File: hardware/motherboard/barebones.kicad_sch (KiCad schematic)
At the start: 0 parts

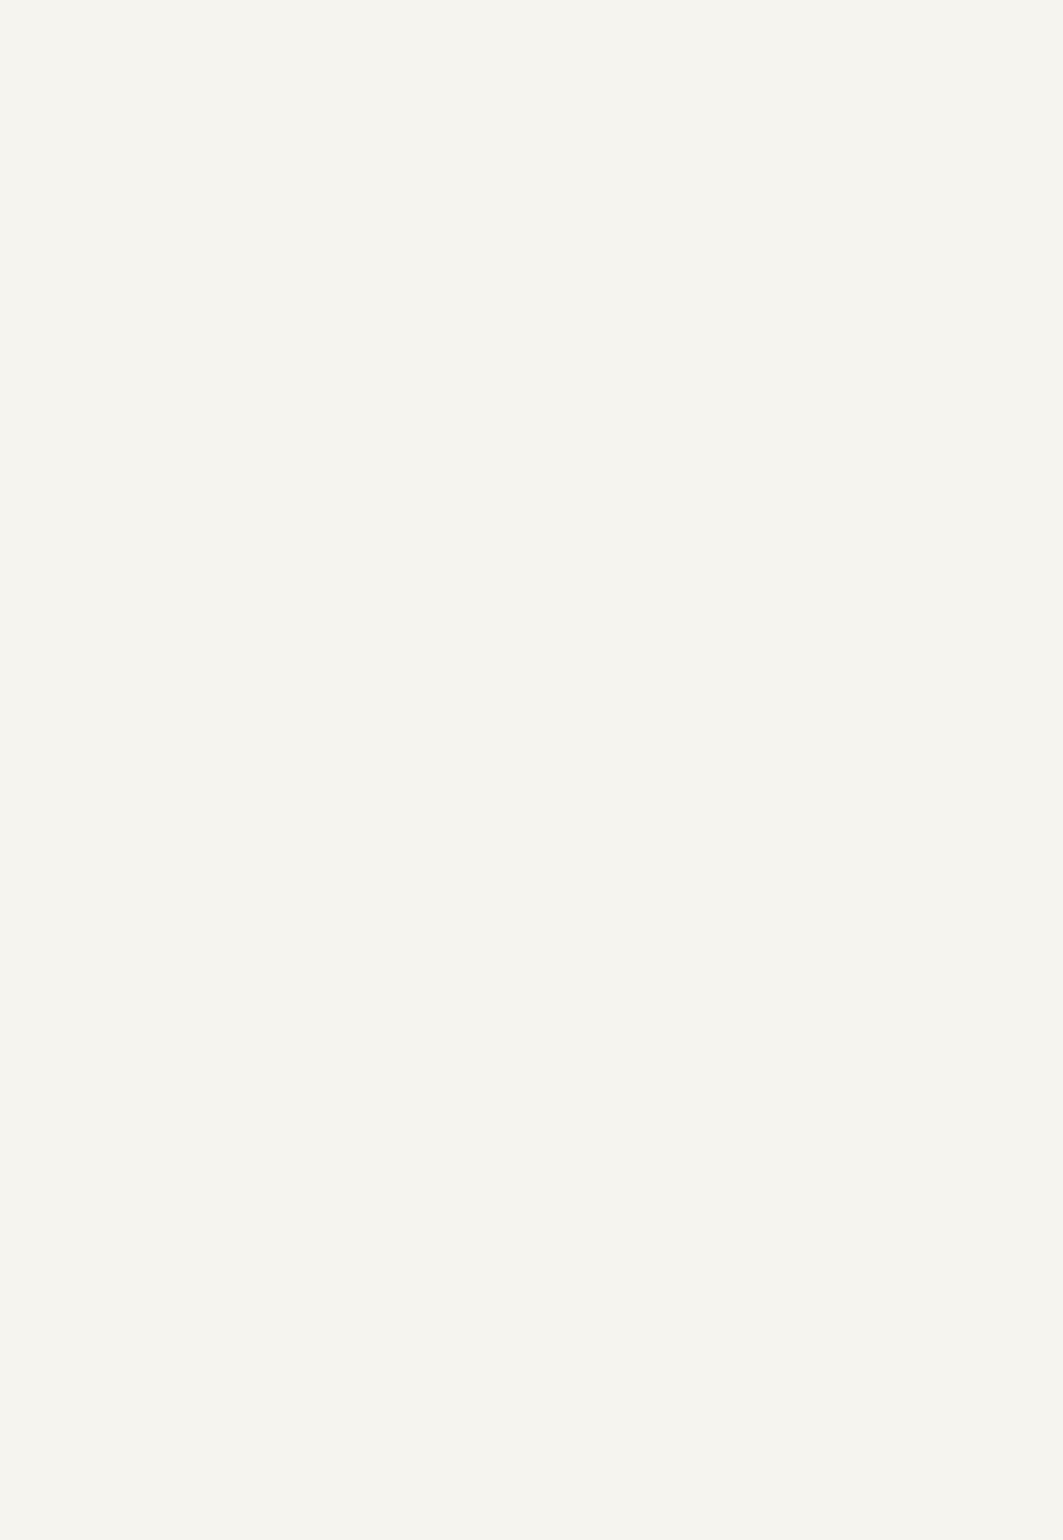
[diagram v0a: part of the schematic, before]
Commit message: pushed many changes and added dedicated bms module
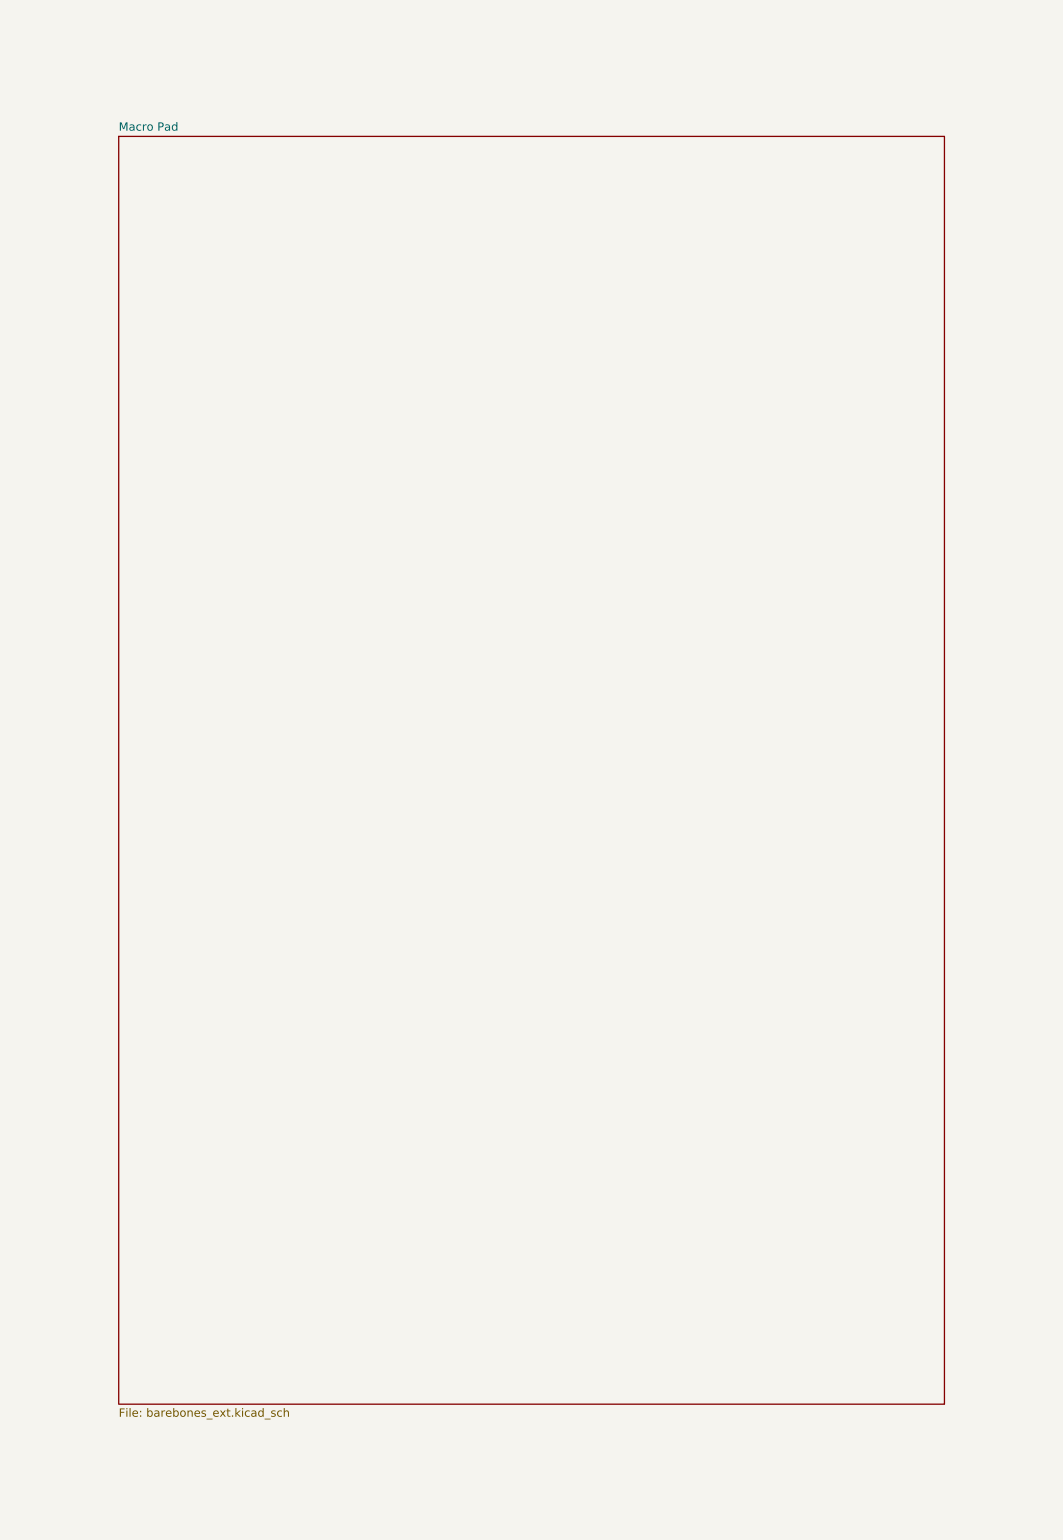
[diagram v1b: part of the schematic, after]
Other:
- added sheet Macro Pad (barebones_ext.kicad_sch)
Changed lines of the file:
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@@
+	)
+	(sheet
+		(at 469.9 403.86)
+		(size 125.73 193.04)
+		(exclude_from_sim no)
+		(in_bom yes)
+		(on_board yes)
+		(dnp no)
+		(fields_autoplaced yes)
+		(stroke
+			(width 0.1524)
+			(type solid)
+		)
+		(fill
+			(color 0 0 0 0)
+		)
+		(property "Sheetname" "Macro Pad"
+			(at 469.9 403.1484 0)
+			(show_name no)
+			(do_not_autoplace no)
+			(effects
+				(font
+					(size 1.27 1.27)
+				)
+				(justify left bottom)
+			)
+		)
+		(property "Sheetfile" "barebones_ext.kicad_sch"
+			(at 469.9 597.4846 0)
+			(show_name no)
+			(do_not_autoplace no)
+			(effects
+				(font
+					(size 1.27 1.27)
+				)
+				(justify left top)
+			)
+		)
+		(instances
+			(project "barebones"
+				(path "/55e8bb80-206a-472b-ac89-6555b6c3d282"
+					(page "8")
+				)
+			)
+		)
 	)
 	(sheet

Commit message: connected hierarchical labels with net labels in the root sheet
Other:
- sheet Embedded Controller and Internal Audio ports: added BACKLIGHT_PWM, BUCK_PWRON, CAPS_P, CHARGE_CNTRL, CHRG_12C_SCL, CHRG_12C_SDA, CHRG_OK_EC, CHRG_PROT, HALL_SENSE, I2C1_SCL_EC, I2C1_SCL_M2, I2C1_SDA_EC, I2C1_SDA_M2, I2C7_SCL_M0, I2C7_SDA_M0, I2S0_LRCK, I2S0_MLCK, I2S0_SCLK, I2S0_SDI0, I2S0_SDO0, INT_AUDIO, KSI0, KSI1, KSI2, KSI3, KSI4, KSI5, KSI6, KSI7, KSO0, KSO1, KSO10, KSO11, KSO12, KSO13, KSO14, KSO15, KSO2, KSO3, KSO4, KSO5, KSO6, KSO7, KSO8, KSO9, MIC_PRESENT, PWRON_RK, RESETB_RK, SMBC_BATT, SMBD_BATT, SPK_MUTE, USB_CTRL_RESET_1, USB_CTRL_RESET_2, USB_SIG_STAT; removed none
- sheet High Speed IO ports: added CPU_BIG0_VSEL, CPU_BIG1_VSEL, DDR_CH1_CK_C, DDR_CH1_CK_D, DDR_CH1_DM0_C, DDR_CH1_DM0_D, DDR_CH1_DM1_C, DDR_CH1_DM1_D, DDR_CH1_DQ0_C, DDR_CH1_DQ0_D, DDR_CH1_DQ10_C, DDR_CH1_DQ10_D, DDR_CH1_DQ11_C, DDR_CH1_DQ11_D, DDR_CH1_DQ12_C, DDR_CH1_DQ12_D, DDR_CH1_DQ13_C, DDR_CH1_DQ13_D, DDR_CH1_DQ14_C, DDR_CH1_DQ14_D, DDR_CH1_DQ15_C, DDR_CH1_DQ15_D, DDR_CH1_DQ1_C, DDR_CH1_DQ1_D, DDR_CH1_DQ2_C, DDR_CH1_DQ2_D, DDR_CH1_DQ3_C, DDR_CH1_DQ3_D, DDR_CH1_DQ4_C, DDR_CH1_DQ4_D, DDR_CH1_DQ5_C, DDR_CH1_DQ5_D, DDR_CH1_DQ6_C, DDR_CH1_DQ6_D, DDR_CH1_DQ7_C, DDR_CH1_DQ7_D, DDR_CH1_DQ8_C, DDR_CH1_DQ8_D, DDR_CH1_DQ9_C, DDR_CH1_DQ9_D, DDR_CH1_DQS0N_C, DDR_CH1_DQS0N_D, DDR_CH1_DQS0P_C, DDR_CH1_DQS0P_D, DDR_CH1_DQS1N_C, DDR_CH1_DQS1N_D, DDR_CH1_DQS1P_C, DDR_CH1_DQS1P_D, DDR_CH1_LP4/4X_CKE0/LP5_CS0_C, DDR_CH1_LP4/4X_CKE0/LP5_CS0_D, DDR_CH1_LP4/4X_CKE1/LP5_CS1_C, DDR_CH1_LP4/4X_CKE1/LP5_CS1_D, DDR_CH1_LP4/4X_CS0_C, DDR_CH1_LP4/4X_CS0_D, DDR_CH1_LP4/4X_CS1_C, DDR_CH1_LP4/4X_CS1_D, DDR_RESET, EDP_TX0_HDP, FSPI-CLK, FSPI-CS0, FSPI-D0, FSPI-D1, FSPI-D2, FSPI-D3, GPIO3_B3_U, GPIO3_B4_U, GPIO3_B5_U, HDMI0_TX0N_PORT/eDP0_TX_D0N, HDMI0_TX0P_PORT/eDP0_TX_D0P, HDMI0_TX1N_PORT/eDP0_TX_D1N, HDMI0_TX1P_PORT/eDP0_TX_D1P, HDMI0_TX2N_PORT/eDP0_TX_D2N, HDMI0_TX2P_PORT/eDP0_TX_D2P, HDMI0_TX3N_PORT/eDP0_TX_D3N, HDMI0_TX3P_PORT/eDP0_TX_D3P, HDMI1_TX0N_PORT/eDP1_TX_D0N, HDMI1_TX0P_PORT/eDP1_TX_D0P, HDMI1_TX1N_PORT/eDP1_TX_D1N, HDMI1_TX1P_PORT/eDP1_TX_D1P, HDMI1_TX2N_PORT/eDP1_TX_D2N, HDMI1_TX2P_PORT/eDP1_TX_D2P, HDMI1_TX3N_PORT/eDP1_TX_D3N, HDMI1_TX3P_PORT/eDP1_TX_D3P, HDMI1_TX_ON_H, HDMI1_TX_SBDN/eDP1_TX_AUXN, HDMI1_TX_SBDP/eDP1_TX_AUXP, HDMITX1_CEC_M2, HDMITX1_HPDIN_M1, HDMITX1_SCL_M1, HDMITX1_SDA_M1, HP_DETECT, HP_INT, I2C0_SCL_M2, I2C0_SDA_M2, I2C1_SCL_M0, I2C1_SDA_M0, I2C4_SCL_M1, I2C4_SDA_M1, I2C4_SDA_M3, I2C5_SCL_M4, I2C5_SDA_M4, I2C7_SCL_M0, I2C7_SDA_M0, I2S0_LRCK_TX, I2S0_MLCK, I2S0_SCLK_TX, I2S0_SDI0, I2S0_SDO0, NPU_VSEL, PCIE20_0_REFCLKN, PCIE20_0_REFCLKP, PCIE20_0_RXN, PCIE20_0_RXP, PCIE20_0_TXN, PCIE20_0_TXP, PCIE30X1_0_CLKREQn_M1_L, PCIE30X1_0_PERSTn_M1_L, PCIE30X1_0_WAKEn_M1_L, PCIE30X2_CLKREQn_M1, PCIE30X2_PERSTn_M1, PCIE30X2_WAKEn_M1, PCIE30X4_CLKREQn_M1_L, PCIE30X4_PERSTn_M1_L, PCIE30X4_PWREN_H, PCIE30X4_WAKEn_M1_L, PCIE30_PORT0_REF_CLKN, PCIE30_PORT0_REF_CLKP, PCIE30_PORT0_RX0N, PCIE30_PORT0_RX0P, PCIE30_PORT0_RX1N, PCIE30_PORT0_RX1P, PCIE30_PORT0_TX0N, PCIE30_PORT0_TX0P, PCIE30_PORT0_TX1N, PCIE30_PORT0_TX1P, PCIE30_PORT1_REF_CLKN, PCIE30_PORT1_REF_CLKP, PCIE30_PORT1_RX0N, PCIE30_PORT1_RX0P, PCIE30_PORT1_RX1N, PCIE30_PORT1_RX1P, PCIE30_PORT1_TX0N, PCIE30_PORT1_TX0P, PCIE30_PORT1_TX1N, PCIE30_PORT1_TX1P, PMIC_INT_L, PMIC_SLEEP1, PWRCTRL2_PMIC, PWRCTRL3_PMIC, RESETB, RTC_CLK_EN, SDMMC_CLK, SDMMC_CMD, SDMMC_DAT0, SDMMC_DAT1, SDMMC_DAT2, SDMMC_DAT3, SDMMC_DET, SPI2_CLK_M2, SPI2_CS0_M2, SPI2_MOSI_M2, USB20_HOST0_DM, USB20_HOST0_DP, USB20_HOST1_DM, USB20_HOST1_DP, USB30_2_SSRXN, USB30_2_SSRXP, USB30_2_SSTXN, USB30_2_SSTXP, USB_1_OTG_DM, USB_1_OTG_DP, USB_1_RX1N, USB_1_RX1P, USB_1_RX2N, USB_1_RX2P, USB_1_SBU1, USB_1_SBU1_DC, USB_1_SBU2, USB_1_TX1N, USB_1_TX1P, USB_1_TX2N, USB_1_TX2P, USB_2_OTG_DM, USB_2_OTG_DP, USB_2_RX1N, USB_2_RX1P, USB_2_RX2N, USB_2_RX2P, USB_2_SBU1, USB_2_SBU1_DC, USB_2_SBU2, USB_2_TX1N, USB_2_TX1P, USB_2_TX2N, USB_2_TX2P; removed none
- sheet Macro Pad ports: added USB_MACRO_DN, USB_MACRO_DP; removed none
- sheet Memory Subsystem(LPDDR4x) ports: added DDR_CH0_A0_A, DDR_CH0_A0_B, DDR_CH0_A1_A, DDR_CH0_A1_B, DDR_CH0_A2_A, DDR_CH0_A2_B, DDR_CH0_A3_A, DDR_CH0_A3_B, DDR_CH0_A4_A, DDR_CH0_A4_B, DDR_CH0_A5_A, DDR_CH0_A5_B, DDR_CH0_CKB_A, DDR_CH0_CKB_B, DDR_CH0_CK_A, DDR_CH0_CK_B, DDR_CH0_DM0_A, DDR_CH0_DM0_B, DDR_CH0_DM1_A, DDR_CH0_DM1_B, DDR_CH0_DQ0_A, DDR_CH0_DQ0_B, DDR_CH0_DQ10_A, DDR_CH0_DQ10_B, DDR_CH0_DQ11_A, DDR_CH0_DQ11_B, DDR_CH0_DQ12_A, DDR_CH0_DQ12_B, DDR_CH0_DQ13_A, DDR_CH0_DQ13_B, DDR_CH0_DQ14_A, DDR_CH0_DQ14_B, DDR_CH0_DQ15_A, DDR_CH0_DQ15_B, DDR_CH0_DQ1_A, DDR_CH0_DQ1_B, DDR_CH0_DQ2_A, DDR_CH0_DQ2_B, DDR_CH0_DQ3_A, DDR_CH0_DQ3_B, DDR_CH0_DQ4_A, DDR_CH0_DQ4_B, DDR_CH0_DQ5_A, DDR_CH0_DQ5_B, DDR_CH0_DQ6_A, DDR_CH0_DQ6_B, DDR_CH0_DQ7_A, DDR_CH0_DQ7_B, DDR_CH0_DQ8_A, DDR_CH0_DQ8_B, DDR_CH0_DQ9_A, DDR_CH0_DQ9_B, DDR_CH0_DQS0N_A, DDR_CH0_DQS0N_B, DDR_CH0_DQS0P_A, DDR_CH0_DQS0P_B, DDR_CH0_DQS1N_A, DDR_CH0_DQS1N_B, DDR_CH0_DQS1P_A, DDR_CH0_DQS1P_B, DDR_CH0_LP4/4X_CKE0/LP5_CS0_A, DDR_CH0_LP4/4X_CKE0/LP5_CS0_B, DDR_CH0_LP4/4X_CKE1/LP5_CS1_A, DDR_CH0_LP4/4X_CKE1/LP5_CS1_B, DDR_CH0_LP4/4X_CS0_A, DDR_CH0_LP4/4X_CS0_B, DDR_CH0_LP4/4X_CS1_A, DDR_CH0_LP4/4X_CS1_B, DDR_CH1_A0_C, DDR_CH1_A0_D, DDR_CH1_A1_C, DDR_CH1_A1_D, DDR_CH1_A2_C, DDR_CH1_A2_D, DDR_CH1_A3_C, DDR_CH1_A3_D, DDR_CH1_A4_C, DDR_CH1_A4_D, DDR_CH1_A5_C, DDR_CH1_A5_D, DDR_CH1_CKB_C, DDR_CH1_CKB_D, DDR_CH1_CK_C, DDR_CH1_CK_D, DDR_CH1_DM0_C, DDR_CH1_DM0_D, DDR_CH1_DM1_C, DDR_CH1_DM1_D, DDR_CH1_DQ0_C, DDR_CH1_DQ0_D, DDR_CH1_DQ10_C, DDR_CH1_DQ10_D, DDR_CH1_DQ11_C, DDR_CH1_DQ11_D, DDR_CH1_DQ12_C, DDR_CH1_DQ12_D, DDR_CH1_DQ13_C, DDR_CH1_DQ13_D, DDR_CH1_DQ14_C, DDR_CH1_DQ14_D, DDR_CH1_DQ15_C, DDR_CH1_DQ15_D, DDR_CH1_DQ1_C, DDR_CH1_DQ1_D, DDR_CH1_DQ2_C, DDR_CH1_DQ2_D, DDR_CH1_DQ3_C, DDR_CH1_DQ3_D, DDR_CH1_DQ4_C, DDR_CH1_DQ4_D, DDR_CH1_DQ5_C, DDR_CH1_DQ5_D, DDR_CH1_DQ6_C, DDR_CH1_DQ6_D, DDR_CH1_DQ7_C, DDR_CH1_DQ7_D, DDR_CH1_DQ8_C, DDR_CH1_DQ8_D, DDR_CH1_DQ9_C, DDR_CH1_DQ9_D, DDR_CH1_DQS0N_C, DDR_CH1_DQS0N_D, DDR_CH1_DQS0P_C, DDR_CH1_DQS0P_D, DDR_CH1_DQS1N_C, DDR_CH1_DQS1N_D, DDR_CH1_DQS1P_C, DDR_CH1_DQS1P_D, DDR_CH1_LP4/4X_CKE0/LP5_CS0_C, DDR_CH1_LP4/4X_CKE0/LP5_CS0_D, DDR_CH1_LP4/4X_CKE1/LP5_CS1_C, DDR_CH1_LP4/4X_CKE1/LP5_CS1_D, DDR_CH1_LP4/4X_CS0_C, DDR_CH1_LP4/4X_CS0_D, DDR_CH1_LP4/4X_CS1_C, DDR_CH1_LP4/4X_CS1_D, DDR_RESET; removed none
- sheet Memory and Control ports: added FSPI-CLK, FSPI-CS0, FSPI-D0, FSPI-D1, FSPI-D2, FSPI-D3, HALL_SENSE_0, I2C1_SCL_M2, I2C1_SDA_M2, LP_INDICATOR, RTC_CLK_EN; removed none
- sheet Peripheral IO Connectors ports: added 12C1_EXTI_EC, BACKLIGHT_DN, BACKLIGHT_DP, BOARD_ID, CAPS_N, CAPS_P, EC_CONTROL, EDP_TX0_AUX_N, EDP_TX0_AUX_P, EDP_TX0_BL_EN, EDP_TX0_BL_PWM, EDP_TX0_HDP, GPIO3_B5_U, HDMI0_TX0N_PORT/eDP0_TX_D0N, HDMI0_TX0P_PORT/eDP0_TX_D0P, HDMI0_TX1N_PORT/eDP0_TX_D1N, HDMI0_TX1P_PORT/eDP0_TX_D1P, HDMI0_TX2N_PORT/eDP0_TX_D2N, HDMI0_TX2P_PORT/eDP0_TX_D2P, HDMI0_TX3N_PORT/eDP0_TX_D3N, HDMI0_TX3P_PORT/eDP0_TX_D3P, HDMI1_TX0N_PORT/eDP1_TX_D0N, HDMI1_TX0P_PORT/eDP1_TX_D0P, HDMI1_TX1N_PORT/eDP1_TX_D1N, HDMI1_TX1P_PORT/eDP1_TX_D1P, HDMI1_TX2N_PORT/eDP1_TX_D2N, HDMI1_TX2P_PORT/eDP1_TX_D2P, HDMI1_TX3N_PORT/eDP1_TX_D3N, HDMI1_TX3P_PORT/eDP1_TX_D3P, HDMI1_TX_ON_H, HDMI1_TX_SBDN/eDP1_TX_AUXN, HDMI1_TX_SBDP/eDP1_TX_AUXP, HDMITX1_CEC_M2, HDMITX1_HPDIN_M1, HDMITX1_SCL_M1, HDMITX1_SDA_M1, I2C1_SCL_EC, I2C1_SDA_EC, KSI0, KSI1, KSI2, KSI3, KSI4, KSI5, KSI6, KSI7, KSO0, KSO1, KSO10, KSO11, KSO12, KSO13, KSO14, KSO15, KSO2, KSO3, KSO4, KSO5, KSO6, KSO7, KSO8, KSO9, PCIE30X1_0_CLKREQn_M1_L, PCIE30X1_0_PERSTn_M1_L, PCIE30X1_0_WAKEn_M1_L, PCIE30X2_CLKREQn_M1, PCIE30X2_PERSTn_M1, PCIE30X2_WAKEn_M1, PCIE30X4_CLKREQn_M1_L, PCIE30X4_PERSTn_M1_L, PCIE30X4_WAKEn_M1_L, PCIE30_PORT0_RX1N, PCIE30_PORT1_REF_CLKN, PCIE30_PORT1_REF_CLKP, PCIE30_REFCLKN_SLOT_0, PCIE30_REFCLKN_SLOT_1, PCIE30_REFCLKP_SLOT_0, PCIE30_REFCLKP_SLOT_1, SDMMC_CLK, SDMMC_CMD, SDMMC_DAT0, SDMMC_DAT1, SDMMC_DAT2, SDMMC_DAT3, SDMMC_DET, SYS_PWR, TP_INT, TP_SCL, TP_SDA, USB20_HOST0_DM, USB20_HOST1_DM, USB20_HOST1_DP, USB30_2_SSRXN, USB30_2_SSRXP, USB30_2_SSTXN, USB30_2_SSTXP, USB30_HUB_RST, USB_1_OTG_DM, USB_1_OTG_DP, USB_1_RX1N, USB_1_RX1P, USB_1_RX2N, USB_1_RX2P, USB_1_SBU1, USB_1_SBU1_DC, USB_1_SBU2, USB_1_TX1N, USB_1_TX1P, USB_1_TX2N, USB_1_TX2P, USB_2_OTG_DM, USB_2_OTG_DP, USB_2_RX1N, USB_2_RX1P, USB_2_RX2N, USB_2_RX2P, USB_2_SBU1, USB_2_SBU1_DC, USB_2_SBU2, USB_2_TX1N, USB_2_TX1P, USB_2_TX2N, USB_2_TX2P, USB_CTRL_RESET, USB_MACRO_DN, USB_MACRO_DP; removed BATT_CHARGER_BQ25713A, I2C2_SCL_M4, I2C2_SDA_M4, PCIE30X1_0_PERSTN_M0, PCIE30X1_0_WAKEN_M0, PCIE30X4_CLKREQN_M0, PCIE30X4_PERSTN_M0, SD_CLK, SD_CMD, SD_DAT0, SD_DAT1, SD_DAT2, SD_DAT3, SD_DETECT, TYPEC0_SBU1, TYPEC0_SSRX1N/DP0_TX0N, TYPEC0_SSRX1P/DP0_TX0P, TYPEC0_SSRX2N/DP0_RX2N, TYPEC0_SSRX2P/DP0_RX2P, TYPEC0_SSTX1N/DP0_TX1N, TYPEC0_SSTX1P/DP0_TX1P, TYPEC0_SSTX2N/DP0_TX3N, TYPEC0_SSTX2P/DP0_TX3P, TYPEC0_USB20_OTG_DM, TYPEC0_USB20_OTG_DP, USB20_HOST0_DN
- sheet Power and Ground ports: added BACKLIGHT_DN, BACKLIGHT_DP, BACKLIGHT_PWM, BUCK_PWRON, CHRG_12C_SCL, CHRG_12C_SDA, CHRG_CTRL, CHRG_OK_EC, CHRG_PROT, CPU_BIG0_VSEL, CPU_BIG1_VSEL, EDP_PWM11_M1, I2C0_SCL_M2, I2C0_SDA_M2, I2C1_SCL_M0, I2C1_SDA_M0, NPU_VSEL, PCIE30X4_PWREN_H, PMIC_INT_L, PMIC_SLEEP1, PWRCTRL2_PMIC, PWRCTRL3_PMIC, PWRON, RESETB, SMBC_BATT, SMBD_BATT, SPI2_CLK_M2, SPI2_CS0_M2, SPI2_MOSI_M2, SYS_PWR; removed none
- note added: "REVIEW EACH CONNECTION BEFORE ROUTING"

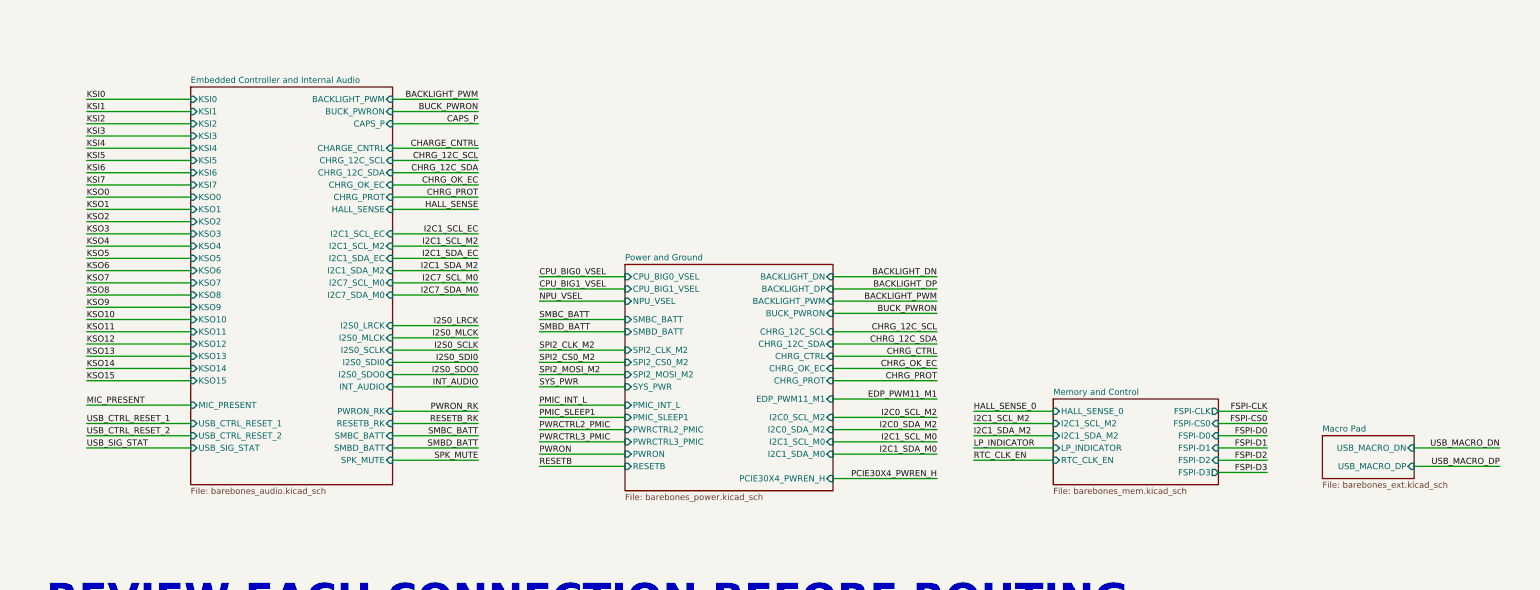
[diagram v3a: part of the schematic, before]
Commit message: removed unused components and connections
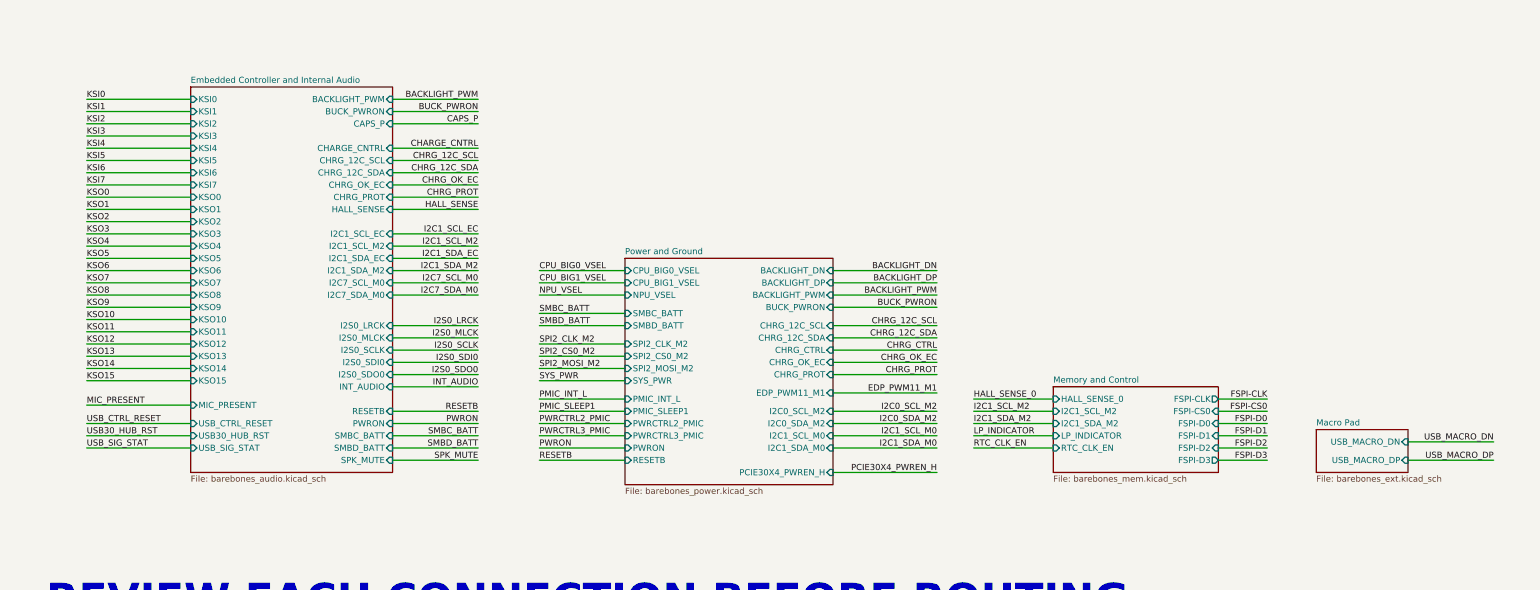
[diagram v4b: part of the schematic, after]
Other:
- sheet Embedded Controller and Internal Audio ports: added PWRON, RESETB, USB30_HUB_RST, USB_CTRL_RESET; removed PWRON_RK, RESETB_RK, USB_CTRL_RESET_1, USB_CTRL_RESET_2

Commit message: updated last changes
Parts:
- added H1, H2, H3, H4, H5: MountingHole_Pad, MountingHole:MountingHole_2.2mm_M2_Pad_Via, symbol Mechanical:MountingHole_Pad
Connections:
- new net GND: H1.1, H2.1, H3.1, H4.1, H5.1
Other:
- sheet Embedded Controller and Internal Audio ports: added AUDIO_PWR_1, AUDIO_PWR_2, BATT_PRES, BK_0_PG, BK_1_PG, CHRG_CTRL, HLL_SENSOR, INT_ALS, LP_INDICATOR; removed CHARGE_CNTRL
- sheet High Speed IO ports: added I2C3_SCL_M0, I2C3_SDA_M0, MIC_CLK, MIC_DAT; removed none
- sheet Memory and Control ports: added AUDIO_PWR_1, AUDIO_PWR_2, HLL_SENSOR, PCIE30X1_B_EN, PCIE30X1_W_EN, PCIE30X4_PWREN_H_EN_1, PCIE30X4_PWREN_H_EN_2, WEBCAM_PWR; removed HALL_SENSE_0
- sheet Peripheral IO Connectors ports: added CAM_SW, I2C3_SCL_M0, I2C3_SDA_M0, INT_ALS, MIC_CLK, MIC_DAT, MIC_SW, PCIE30X1_B_EN, PCIE30X1_W_EN, SCL_ALS, SDA_ALS, WEBCAM_EN, WEBCAM_PWR; removed none
- sheet Power and Ground ports: added BATT_PRES, BK_0_PG, BK_1_PG, PCIE30X4_PWREN_H_EN_1, PCIE30X4_PWREN_H_EN_2; removed none

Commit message: started routing on LPDDR4x RAM
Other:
- sheet Embedded Controller and Internal Audio ports: added 12C1_EXTI_EC; removed none
- sheet High Speed IO ports: added CAM_SW, DDR_CH1_CK_C_N, DDR_CH1_CK_C_P, DDR_CH1_CK_D_N, DDR_CH1_CK_D_P, DDR_CH1_DQS0_C_N, DDR_CH1_DQS0_C_P, DDR_CH1_DQS0_D_N, DDR_CH1_DQS0_D_P, DDR_CH1_DQS1_C_N, DDR_CH1_DQS1_C_P, DDR_CH1_DQS1_D_N, DDR_CH1_DQS1_D_P, I2C8_SCL_M2, I2C8_SDA_M2, INT_ALS, MIC_SW, USB_1_OTG_DN, USB_2_OTG_DN; removed DDR_CH1_CKB_C, DDR_CH1_CKB_D, DDR_CH1_CK_C, DDR_CH1_CK_D, DDR_CH1_DQS0N_C, DDR_CH1_DQS0N_D, DDR_CH1_DQS0P_C, DDR_CH1_DQS0P_D, DDR_CH1_DQS1N_C, DDR_CH1_DQS1N_D, DDR_CH1_DQS1P_C, DDR_CH1_DQS1P_D, I2C3_SCL_M0, I2C3_SDA_M0, USB_1_OTG_DM, USB_2_OTG_DM
- sheet Memory Subsystem(LPDDR4x) ports: added DDR_CH1_CK_C_N, DDR_CH1_CK_C_P, DDR_CH1_CK_D_N, DDR_CH1_CK_D_P, DDR_CH1_DQS0_C_N, DDR_CH1_DQS0_C_P, DDR_CH1_DQS0_D_N, DDR_CH1_DQS0_D_P, DDR_CH1_DQS1_C_N, DDR_CH1_DQS1_C_P, DDR_CH1_DQS1_D_N, DDR_CH1_DQS1_D_P; removed DDR_CH1_CKB_C, DDR_CH1_CKB_D, DDR_CH1_CK_C, DDR_CH1_CK_D, DDR_CH1_DQS0N_C, DDR_CH1_DQS0N_D, DDR_CH1_DQS0P_C, DDR_CH1_DQS0P_D, DDR_CH1_DQS1N_C, DDR_CH1_DQS1N_D, DDR_CH1_DQS1P_C, DDR_CH1_DQS1P_D
- sheet Peripheral IO Connectors ports: added USB_1_OTG_DN, USB_2_OTG_DN; removed USB_1_OTG_DM, USB_2_OTG_DM
- sheet Power and Ground ports: added none; removed EDP_PWM11_M1
- moved on the sheet: H1, H2, H3, H4
